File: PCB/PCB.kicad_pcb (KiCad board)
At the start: 2 copper layers, 270.3 x 90.2 mm, 156 parts, among them J1 R_Motor, J10 Servos, J11 PWR-Servos, J12 R-INMP441, J13 Debug, J14 Raspberry_Pi_Zero, J15 F_HS-SR04+, J16 B_HS-SR04+, J17 MPU-6050, J18 12v 20Ah Battery, J19 Free_GPIO, J2 USB_C_Receptacle_USB2.0_16P, J3 Left_Speaker, J4 Right_Speaker, J5 GAIN_sel, J6 L_Motor, J7 Servos, J8 Servos, J9 Servos, Q1 AOD417, SW1 SW_MEC_5E, SW2 SW_MEC_5E, SW3 SW_MEC_5E, SW4 Main_Power-SW, U1 ESP32-S3-WROOM-1, U10 BTN7960B, U11 PCA9685PW, U13 MP1584EN-LF-Z, U14 MP1584EN-LF-Z, U16 TFT_320x240, U2 MAX98357A, U3 AMS1117-3.3, U4 MAX98357A, U5 BTN7960B, U6 BTN7960B, U7 74HC244, U8 74HC244, U9 BTN7960B

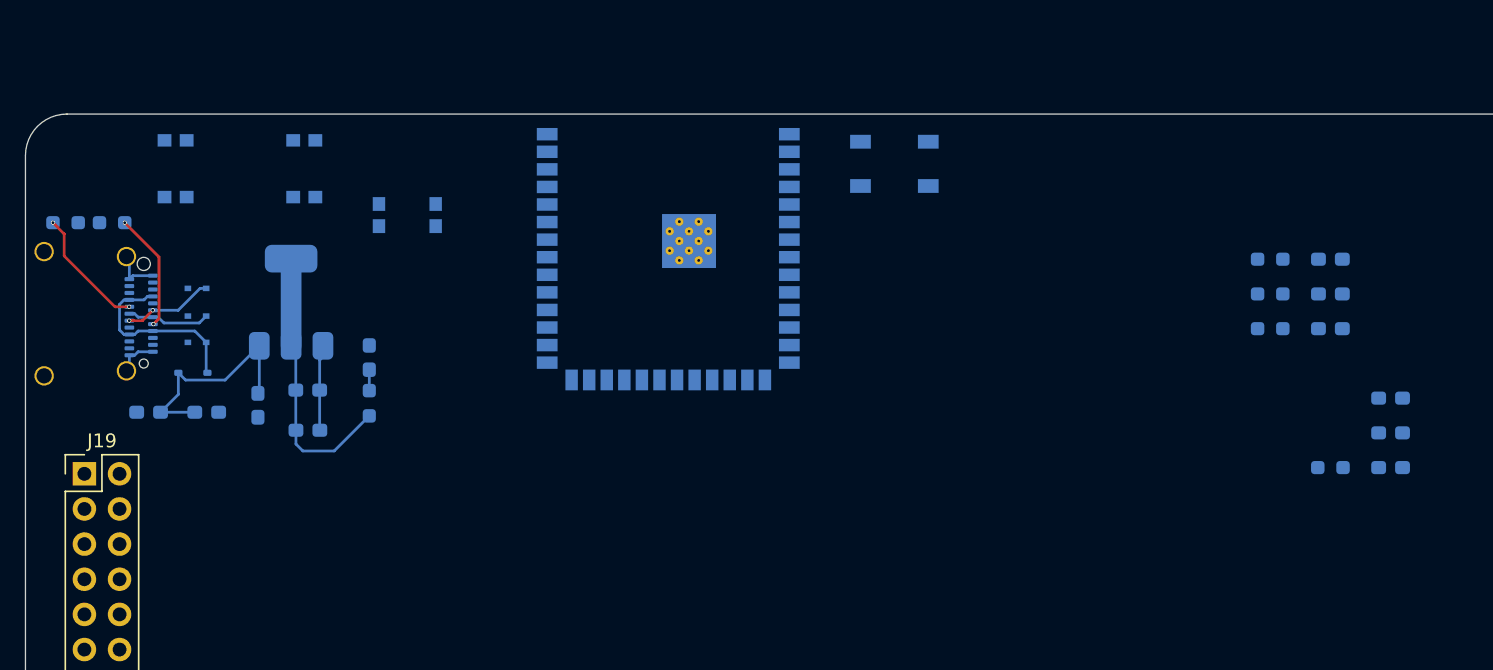
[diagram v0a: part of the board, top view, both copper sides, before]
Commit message: [PCB] Connected BTs & USB to the ESP
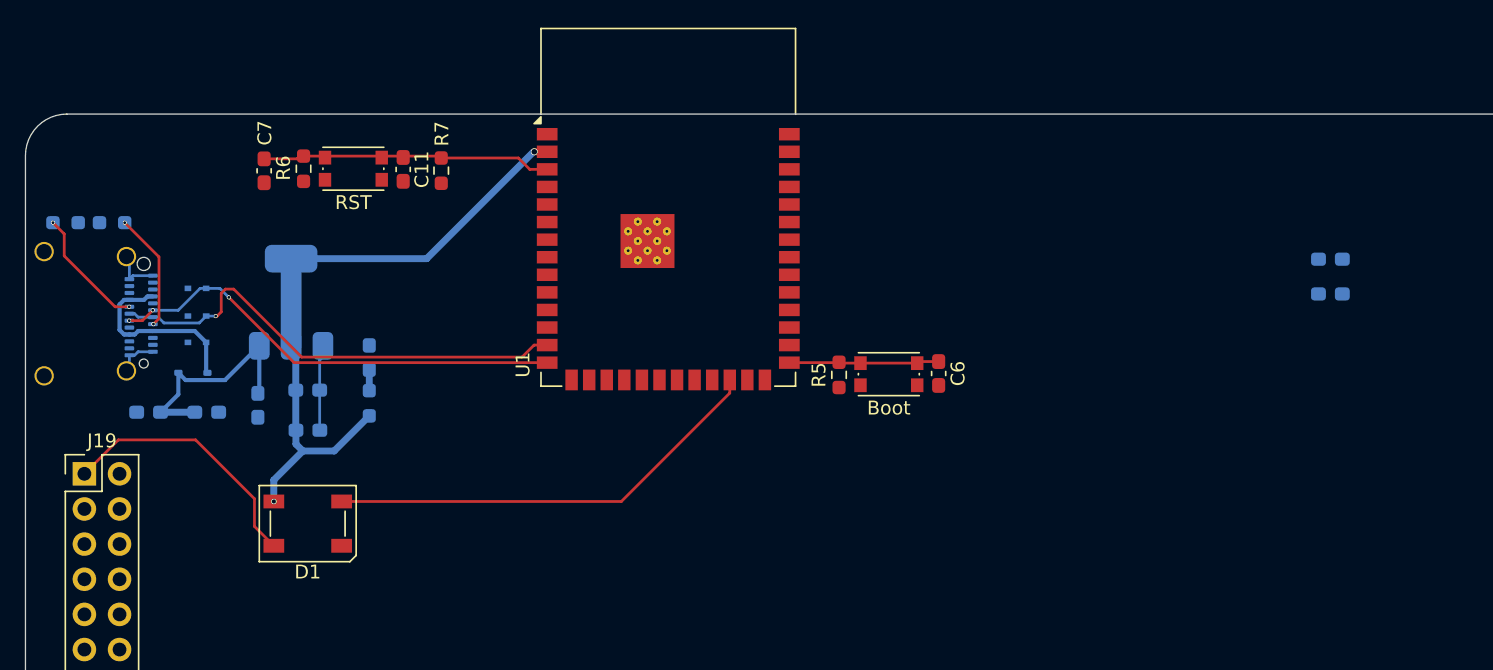
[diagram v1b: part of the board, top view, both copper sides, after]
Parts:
- removed C8: 0.1 uF, Capacitor_SMD:C_0603_1608Metric_Pad1.08x0.95mm_HandSolder
- removed R8: 10k, Resistor_SMD:R_0603_1608Metric_Pad0.98x0.95mm_HandSolder
- removed SW3: SW_MEC_5E, RAM:SW_Push_1P1T_NO_CK_KMR2
- Boot: renamed from SW1; moved to F.Cu
- C11, C6, C7, D1, R5, R6, R7, U1: moved to F.Cu
- RST: renamed from SW2; moved to F.Cu
- moved C7 83.6 mm to (30.8, 57.1), turned to -90 degrees
- moved R6 70.2 mm to (33.6, 57.0), turned to -90 degrees
- moved C11 68.0 mm to (40.8, 57.0), turned to -90 degrees
- moved R7 60.6 mm to (43.5, 57.1), turned to -90 degrees
- moved D1 49.7 mm to (33.9, 82.6)
- moved Boot 44.8 mm to (75.9, 71.8), turned to 180 degrees
- moved R5 36.1 mm to (72.3, 71.8), turned to -90 degrees
- moved C6 32.7 mm to (79.5, 71.8), turned to -90 degrees
- moved RST 5.14 mm to (37.2, 57.0)
- turned U1 to 0 degrees
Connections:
- Boot pad 1: unconnected-(SW1-Pad1) -> GND
- Boot pad 2: unconnected-(SW1-Pad2) -> GND
- D1 pad 4: /Brain/RGB -> /RGB
- J19 pad 1: /GPIO0 -> /RGB
- U1 pad 27: /E-GPIO0 -> GPIO_0
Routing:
- net RGB: track 0.00 -> 32.2 mm
- net Dn: track 6.03 -> 34.7 mm, vias 0 -> 1
- net Dp: track 6.57 -> 33.4 mm, vias 2 -> 3
- net +3.3V: track 20.1 -> 46.3 mm, vias 0 -> 2
- net CHIP_PU: track 0.00 -> 20.9 mm
- net /RGB: track 0.00 -> 19.0 mm
- net GPIO_0: track 0.00 -> 10.9 mm

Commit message: [PCB] Traced motors controllers & step downs
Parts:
- removed J11: PWR-Servos, TerminalBlock_Altech:Altech_AK100_1x02_P5.00mm
- removed R24, R25, R26, R27, R32, R33: 0, Resistor_SMD:R_0603_1608Metric_Pad0.98x0.95mm_HandSolder
- removed R39: 10k, Resistor_SMD:R_0603_1608Metric_Pad0.98x0.95mm_HandSolder
- moved J1 344.2 mm to (243.1, 57.0)
- moved U10 327.3 mm to (251.9, 71.3), turned to 90 degrees
- moved U9 310.1 mm to (239.6, 71.3), turned to 90 degrees
- moved J6 292.9 mm to (94.5, 56.9)
- moved Q1 288.8 mm to (214.9, 83.3), turned to 180 degrees
- moved U6 278.6 mm to (239.6, 98.8), turned to 90 degrees
- moved U5 277.7 mm to (251.9, 98.8), turned to 90 degrees
- moved C24 277.6 mm to (218.2, 90.9), turned to -90 degrees
- moved U8 261.8 mm to (262.3, 85.4), turned to 180 degrees
- moved U7 255.4 mm to (262.3, 112.9), turned to 180 degrees
- moved U2 226.5 mm to (115.1, 115.1)
- moved U4 226.5 mm to (115.1, 120.4)
- moved J5 226.5 mm to (120.5, 123.8)
- moved D7 222.2 mm to (110.2, 117.2)
- moved SW4 212.0 mm to (266.1, 65.2)
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- renumbered Boot to SW1, RST to SW2
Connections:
- C24 pad 1: +5VA -> +5VD
- J10 pad 11: +5VA -> +5VD
- J10 pad 2: +5VA -> +5VD
- J10 pad 5: +5VA -> +5VD
- J10 pad 8: +5VA -> +5VD
- J7 pad 11: +5VA -> +5VD
- J7 pad 2: +5VA -> +5VD
- J7 pad 5: +5VA -> +5VD
- J7 pad 8: +5VA -> +5VD
- J8 pad 11: +5VA -> +5VD
- J8 pad 2: +5VA -> +5VD
- J8 pad 5: +5VA -> +5VD
- J8 pad 8: +5VA -> +5VD
- J9 pad 11: +5VA -> +5VD
- J9 pad 2: +5VA -> +5VD
- J9 pad 5: +5VA -> +5VD
- J9 pad 8: +5VA -> +5VD
- Q1 pad 2: Net-(J11-Pin_2) -> +5VA
- Q1 pad 3: +5VA -> +5VD
- U11 pad 1: Net-(U11-A0) -> +5V
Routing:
- net +12V: track 0.00 -> 221.8 mm
- net +5V: track 16.4 -> 204.8 mm
- net /LM-: track 0.00 -> 168.7 mm, vias 0 -> 2
- net /LM+: track 0.00 -> 161.0 mm, vias 0 -> 2
- net +5VD: track 0.00 -> 121.4 mm
- net /GPIO24: track 0.00 -> 70.8 mm
- net /GPIO16: track 0.00 -> 65.6 mm
- net /GPIO26: track 0.00 -> 63.4 mm, vias 0 -> 2
- net /RM+: track 0.00 -> 63.0 mm, vias 0 -> 2
- net /GPIO13: track 0.00 -> 58.4 mm
- net /RM-: track 0.00 -> 55.5 mm, vias 0 -> 2
- net /GPIO12: track 0.00 -> 55.4 mm
- net /GPIO1: track 0.00 -> 51.6 mm
- net /GPIO7: track 0.00 -> 47.1 mm
- net /GPIO25: track 0.00 -> 46.4 mm, vias 0 -> 1
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
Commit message: [PCB] 95% finished the PCB
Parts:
- removed REF** (x2): MountingHole_3.2mm_M3, MountingHole:MountingHole_3.2mm_M3
- J12: value R-INMP441 -> L-INMP441
- moved J17 207.4 mm to (211.6, 56.7)
- moved J15 175.0 mm to (131.3, 56.7)
- moved J16 175.0 mm to (119.5, 56.7)
- moved C16 154.0 mm to (83.5, 126.9), turned to -90 degrees
- moved C15 151.7 mm to (85.0, 126.9), turned to -90 degrees
- moved FB3 150.4 mm to (86.3, 134.8), turned to -90 degrees
- moved FB4 149.7 mm to (87.8, 134.8), turned to -90 degrees
- moved C14 148.6 mm to (83.8, 137.6)
- moved C13 141.5 mm to (90.5, 137.6), turned to 180 degrees
- moved J13 138.5 mm to (78.9, 56.8)
- moved R59 126.0 mm to (140.5, 126.3), turned to 180 degrees
- moved C23 121.8 mm to (245.7, 81.3), turned to -90 degrees
- moved C22 113.3 mm to (259.4, 90.6), turned to -90 degrees
- moved R2 105.7 mm to (136.9, 138.1), turned to 180 degrees
- moved R10 105.7 mm to (136.9, 140.7)
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- renumbered SW1 to BOOT, SW2 to RST
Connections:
- FB3 pad 1: Net-(J3-Pin_2) -> Net-(U4-OUTP)
- FB3 pad 2: Net-(U4-OUTN) -> Net-(J3-Pin_2)
- FB4 pad 1: Net-(U4-OUTP) -> Net-(U4-OUTN)
- FB5 pad 1: Net-(U2-OUTP) -> Net-(U2-OUTN)
- FB6 pad 1: Net-(J4-Pin_2) -> Net-(U2-OUTP)
- FB6 pad 2: Net-(U2-OUTN) -> Net-(J4-Pin_2)
- J12 pad 1: +3.3V -> GND
- J19 pad 10: /E-GPIO3 -> /E-GPIO9
- J19 pad 12: /E-GPIO16 -> /E-GPIO10
- J19 pad 16: /E-GPIO38 -> /E-GPIO39
- J19 pad 18: /E-GPIO39 -> /E-GPIO40
- J19 pad 20: /E-GPIO40 -> /E-GPIO41
- J19 pad 8: /E-GPIO0 -> /E-GPIO3
- U1 pad 12: /F_Trig -> /L_EN_(RM)
- U1 pad 16: /R_EN_(LM) -> /E-GPIO40
- U1 pad 17: /B_Trig -> /E-GPIO9
- U1 pad 18: /F_Echo -> /E-GPIO10
- U1 pad 19: /L_PWM_(LM) -> /R_PWM_(RM)
- U1 pad 20: /R_PWM_(LM) -> /L_PWM_(RM)
- U1 pad 21: /L_PWM_(RM) -> /R_PWM_(LM)
- U1 pad 22: /R_PWM_(RM) -> /L_PWM_(LM)
- U1 pad 25: /L_EN_(LM) -> /E-GPIO39
- U1 pad 26: /R_EN_(RM) -> /E-GPIO41
- U1 pad 31: /E-GPIO38 -> /F_Echo
- U1 pad 32: /E-GPIO39 -> /F_Trig
- U1 pad 33: /E-GPIO40 -> /B_Echo
- U1 pad 34: /L_EN_(RM) -> /B_Trig
- U1 pad 35: /L_EN_(RM) -> /L_EN_(LM)
- U1 pad 8: /B_Echo -> /R_EN_(LM)
- U1 pad 9: /E-GPIO16 -> /R_EN_(RM)
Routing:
- net +3.3V: track 46.3 -> 452.8 mm, vias 2 -> 9
- net /L_PWM_(LM): track 1.96 -> 300.2 mm
- net /R_PWM_(LM): track 2.13 -> 299.1 mm
- net +5V: track 204.8 -> 499.7 mm, vias 0 -> 5
- net /R_IS_(RM): track 3.42 -> 285.1 mm, vias 0 -> 2
- net /L_IS_(RM): track 3.43 -> 282.3 mm, vias 0 -> 2
- net /L_PWM_(RM): track 1.89 -> 275.6 mm
- net /R_PWM_(RM): track 2.04 -> 274.6 mm
- net /R_EN_(LM): track 2.05 -> 258.3 mm, vias 0 -> 2
- net /SCL: track 6.88 -> 252.2 mm, vias 2 -> 6
- net /L_EN_(RM): track 1.93 -> 246.7 mm, vias 0 -> 2
- net /SDA: track 5.58 -> 248.6 mm, vias 2 -> 3
- net /L_IS_(LM): track 3.41 -> 243.1 mm, vias 0 -> 2
- net /R_EN_(RM): track 1.96 -> 241.4 mm, vias 0 -> 2
- net /L_EN_(LM): track 2.05 -> 240.1 mm, vias 0 -> 2
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- added copper zone on B.Cu, net GND
- added copper zone on F.Cu, net GND
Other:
- board text added: "3v3"
- board text added: "EIO10"
- board text added: "EIO21"
- board text added: "EIO3"
- board text added: "EIO39"
- board text added: "EIO40"
- board text added: "EIO41"
- board text added: "EIO9"
- board text added: "EIO=EspGpio"
- board text added: "ESP USB"
- board text added: "IO1"
- board text added: "IO12"
- board text added: "IO13"
- board text added: "IO16"
- board text added: "IO17"
- board text added: "IO2"
- board text added: "IO23"
- board text added: "IO24"
- board text added: "IO25"
- board text added: "IO26"
- board text added: "IO3"
- board text added: "IO7"
- board text added: "IO8"
- board text added: "IO=RasPiGpio"
- board text added: "RGB"

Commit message: [PCB] Finished the PCB
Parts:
- added G***: LOGO, LOGO, F.Cu at (109.8, 97.6)
- added G***: LOGO, LOGO, F.Cu at (270.3, 98.8)
- added G***: LOGO, LOGO, B.Cu at (132.8, 94.3)
- added G***: LOGO, LOGO, B.Cu at (182.2, 97.4)
- J17: value MPU-6050 -> IMU Sensor
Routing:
- net GPIO_0: track 7.31 -> 10.9 mm
- net GND: vias 106 -> 126
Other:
- board text added: "Caution: High Voltage"
- board text added: "F-Usonic"
- board text added: "L-Usonic"
- board text added: "Left_Speaker"
- board text added: "Microphone Connector"
- board text added: "Right_Speaker"
- board text added: "Servo1 ------------> Servo16"

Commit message: [PCB] Splited the PCB into two boards
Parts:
- removed the G*** at (132.8, 94.3)
- removed the G*** at (182.2, 97.4)
- removed U16: TFT_320x240, Display-extra:TFT-320x240
- added ?: , , F.Cu at (126.9, 125.4)
- added J20: Boards_Connector, Connector_JST:JST_ZH_B8B-ZR-SM4-TF_1x08-1MP_P1.50mm_Vertical, F.Cu at (232.7, 108.3)
- added J21: Boards_Connector, Connector_JST:JST_ZH_B8B-ZR-SM4-TF_1x08-1MP_P1.50mm_Vertical, F.Cu at (232.5, 59.8)
- added J22: Boards_Connector, Connector_JST:JST_ZH_B8B-ZR-SM4-TF_1x08-1MP_P1.50mm_Vertical, F.Cu at (125.6, 69.8)
- added J23: Boards_Connector, Connector_JST:JST_ZH_B8B-ZR-SM4-TF_1x08-1MP_P1.50mm_Vertical, F.Cu at (125.4, 113.1)
- added REF**: MountingHole_2.2mm_M2, MountingHole:MountingHole_2.2mm_M2, F.Cu at (253.2, 75.9)
- added REF**: MountingHole_2.2mm_M2, MountingHole:MountingHole_2.2mm_M2, F.Cu at (49.4, 97.7)
- added REF**: MountingHole_2.2mm_M2, MountingHole:MountingHole_2.2mm_M2, F.Cu at (301.6, 129.0)
- added REF**: TestPoint_THTPad_D1.7mm_Drill1.0mm-naked, TestPoint-extra:TestPoint_THTPad_D1.7mm_Drill1.0mm-naked, F.Cu at (231.7, 129.0)
- added REF**: MountingHole_2.2mm_M2, MountingHole:MountingHole_2.2mm_M2, F.Cu at (118.6, 58.0)
- added REF**: MountingHole_2.2mm_M2, MountingHole:MountingHole_2.2mm_M2, F.Cu at (103.1, 121.0)
- added U15: TFT_128x160, Connector_JST:JST_ZH_B8B-ZR-SM4-TF_1x08-1MP_P1.50mm_Vertical, F.Cu at (61.3, 107.8)
- J17: value IMU Sensor -> MPU-6050
- moved J6 160.0 mm to (254.2, 47.1)
- moved R59 106.9 mm to (245.4, 105.4), turned to -90 degrees
- moved D7 104.1 mm to (245.4, 101.7), turned to 90 degrees
- moved R60 98.5 mm to (233.9, 93.8)
- moved C26 96.5 mm to (250.1, 93.2)
- moved C31 96.3 mm to (240.4, 88.8)
- moved C32 96.3 mm to (237.9, 93.7)
- moved D8 96.3 mm to (236.0, 89.0)
- moved L1 96.3 mm to (237.9, 96.9)
- moved R62 96.3 mm to (240.3, 97.8)
- moved R63 96.3 mm to (241.2, 100.2)
- moved R64 96.3 mm to (237.9, 92.2)
- moved U13 96.3 mm to (243.3, 93.0)
- moved C27 96.3 mm to (235.3, 97.8)
- moved R61 96.3 mm to (245.8, 98.1)
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- renumbered BOOT to SW1, RST to SW2
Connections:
- C1 pad 1: +5V -> +5VCo
- C22 pad 1: +5V -> +5VCo
- C25 pad 1: +5V -> +5VCo
- C27 pad 2: +5V -> +5VCo
- D7 pad 2: +5V -> +5VCo
- J14 pad 21: /Dash_MISO -> /Brain/GPIO9
- J14 pad 7: /T_CS -> /Brain/GPIO4
- J17 pad 1: +3.3V -> +3.3VCo
- J17 pad 3: /SCL -> /SCL-Co
- J17 pad 4: /SDA -> /SDA-Co
- L1 pad 1: +5V -> +5VCo
- R13 pad 1: /R_IS_(RM) -> /R_IS_(RM)Co
- R15 pad 1: /R_IS_(LM) -> /R_IS_(LM)Co
- R16 pad 1: /R_PWM_(RM) -> /R_PWM_(RM)Co
- R17 pad 1: /R_EN_(RM) -> /R_EN_(RM)Co
- R18 pad 1: /L_PWM_(RM) -> /L_PWM_(RM)Co
- R19 pad 1: /L_EN_(RM) -> /L_EN_(RM)Co
- R20 pad 1: /R_PWM_(LM) -> /R_PWM_(LM)Co
- R21 pad 1: /R_EN_(LM) -> /R_EN_(LM)Co
- R22 pad 1: /L_PWM_(LM) -> /L_PWM_(LM)Co
- R23 pad 1: /L_EN_(LM) -> /L_EN_(LM)Co
- R28 pad 1: /L_IS_(RM) -> /L_IS_(RM)Co
- R30 pad 1: /L_IS_(LM) -> /L_IS_(LM)Co
- R57 pad 1: +5V -> +5VCo
- R57 pad 2: /SDA -> /SDA-Co
- R58 pad 1: +5V -> +5VCo
- R58 pad 2: /SCL -> /SCL-Co
- R62 pad 1: +5V -> +5VCo
- U10 pad 6: /L_IS_(LM) -> /L_IS_(LM)Co
- U11 pad 1: +5V -> +5VCo
- U11 pad 26: /SCL -> /SCL-Co
- U11 pad 27: /SDA -> /SDA-Co
- U11 pad 28: +5V -> +5VCo
- U5 pad 6: /L_IS_(RM) -> /L_IS_(RM)Co
- U6 pad 6: /R_IS_(RM) -> /R_IS_(RM)Co
- U7 pad 2: /R_PWM_(RM) -> /R_PWM_(RM)Co
- U7 pad 20: +5V -> +5VCo
- U7 pad 4: /R_EN_(RM) -> /R_EN_(RM)Co
- U7 pad 6: /L_PWM_(RM) -> /L_PWM_(RM)Co
- U7 pad 8: /L_EN_(RM) -> /L_EN_(RM)Co
- U8 pad 2: /R_PWM_(LM) -> /R_PWM_(LM)Co
- U8 pad 20: +5V -> +5VCo
- U8 pad 4: /R_EN_(LM) -> /R_EN_(LM)Co
- U8 pad 6: /L_PWM_(LM) -> /L_PWM_(LM)Co
- U8 pad 8: /L_EN_(LM) -> /L_EN_(LM)Co
- U9 pad 6: /R_IS_(LM) -> /R_IS_(LM)Co
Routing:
- net /L_PWM_(LM): track 300.2 -> 64.8 mm
- net +5V: track 499.7 -> 267.2 mm
- net /R_PWM_(LM): track 299.1 -> 90.6 mm
- net /SCL: track 252.2 -> 60.6 mm, vias 6 -> 2
- net /SDA: track 248.6 -> 61.4 mm, vias 3 -> 2
- net /L_PWM_(RM): track 275.6 -> 92.7 mm
- net /L_EN_(LM): track 240.1 -> 59.6 mm
- net /R_PWM_(RM): track 274.6 -> 94.2 mm
- net /R_EN_(LM): track 258.3 -> 79.3 mm
- net /T_CS: track 173.1 -> 0.00 mm, vias 2 -> 0
- net /L_EN_(RM): track 246.7 -> 81.3 mm
- net /R_EN_(RM): track 241.4 -> 79.4 mm
- net /R_IS_(RM): track 285.1 -> 124.4 mm, vias 2 -> 4
- net /Dash_MISO: track 160.3 -> 0.00 mm, vias 2 -> 0
- net /R_IS_(RM)Co: track 0.00 -> 158.9 mm, vias 0 -> 2
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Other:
- board size 270.3 x 90.2 mm -> 292.8 x 100.1 mm

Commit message: [PCB] Connected the boards via cut-holes for manufacturing
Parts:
- added ?: , , F.Cu at (129.8, 83.7)
- added ?: , , F.Cu at (129.8, 126.6)
- added ?: , , F.Cu at (129.8, 63.7)
- added ?: , , F.Cu at (129.8, 85.0)
- added ?: , , F.Cu at (129.8, 86.4)
- added ?: , , F.Cu at (129.8, 65.1)
- added ?: , , F.Cu at (129.8, 62.4)
- added ?: , , F.Cu at (129.8, 125.2)
- added ?: , , F.Cu at (129.8, 82.3)
- added ?: , , F.Cu at (129.8, 61.0)
- added ?: , , F.Cu at (129.8, 127.9)
- added ?: , , F.Cu at (129.8, 129.3)
- added REF**: Cut_hole, Wall_E_FPs:Cut_hole, F.Cu at (129.8, 123.8)
- added REF**: Cut_hole, Wall_E_FPs:Cut_hole, F.Cu at (129.8, 59.6)
- added REF**: Cut_hole, Wall_E_FPs:Cut_hole, F.Cu at (129.8, 80.9)
- moved C21 99.0 mm to (169.7, 108.9)
- moved C23 99.0 mm to (169.7, 81.3)
- moved C24 99.0 mm to (142.2, 90.9)
- moved C27 99.0 mm to (136.8, 107.7)
- moved C31 99.0 mm to (141.9, 98.7)
- moved C32 99.0 mm to (139.4, 103.6)
- moved D8 99.0 mm to (137.5, 98.9)
- moved D9 99.0 mm to (146.2, 70.1)
- moved G*** 99.0 mm to (197.2, 98.5)
- moved J7 99.0 mm to (136.3, 133.8)
- moved J9 99.0 mm to (147.1, 133.8)
- moved L1 99.0 mm to (139.4, 106.8)
- moved L2 99.0 mm to (148.3, 77.7)
- moved R14 99.0 mm to (164.7, 81.4)
- moved R15 99.0 mm to (166.2, 81.4)
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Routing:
- net GND: track 60.7 -> 74.5 mm, vias 110 -> 143
- net /GPIO16: track 65.6 -> 67.2 mm
- net /LM+: vias 2 -> 3
- net (no net): vias 2 -> 0
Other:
- board size 292.8 x 100.1 mm -> 194.3 x 90.2 mm
